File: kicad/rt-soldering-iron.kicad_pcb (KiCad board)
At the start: 2 copper layers, 74.9 x 20.3 mm, 123 parts, among them J1 IRON_TIP, J2 BARREL_JACK, J3 CONN_01X04, Q1 SIA483DJ-T1-GE3, Q2 FDG6301N_F085, Q3 MMBT3904, Q4 MMBT3906WT1G, Q5 FDG6301N_F085, Q6 MMBT3906WT1G, Q7 FDG6301N_F085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

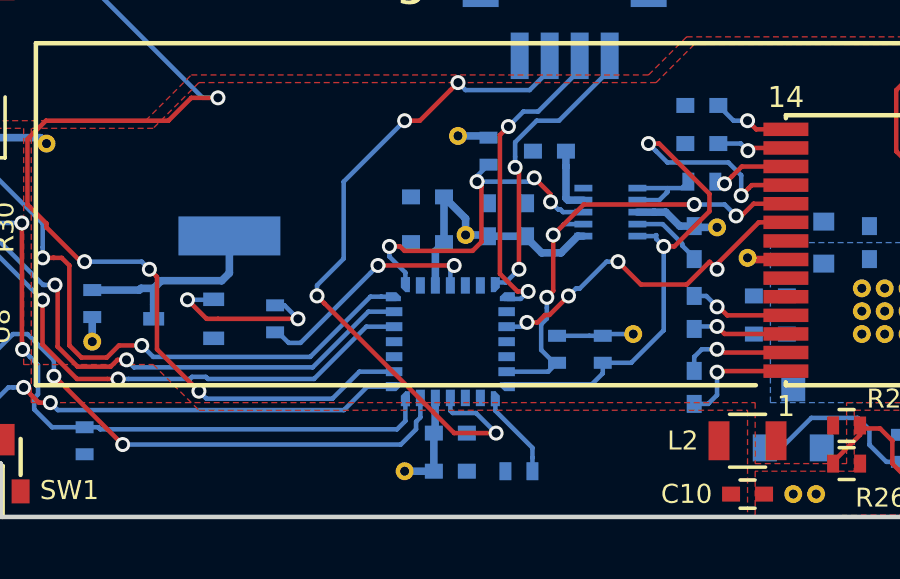
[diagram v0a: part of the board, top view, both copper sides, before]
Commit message: Added tags to unused QFN pins except on accelerometer
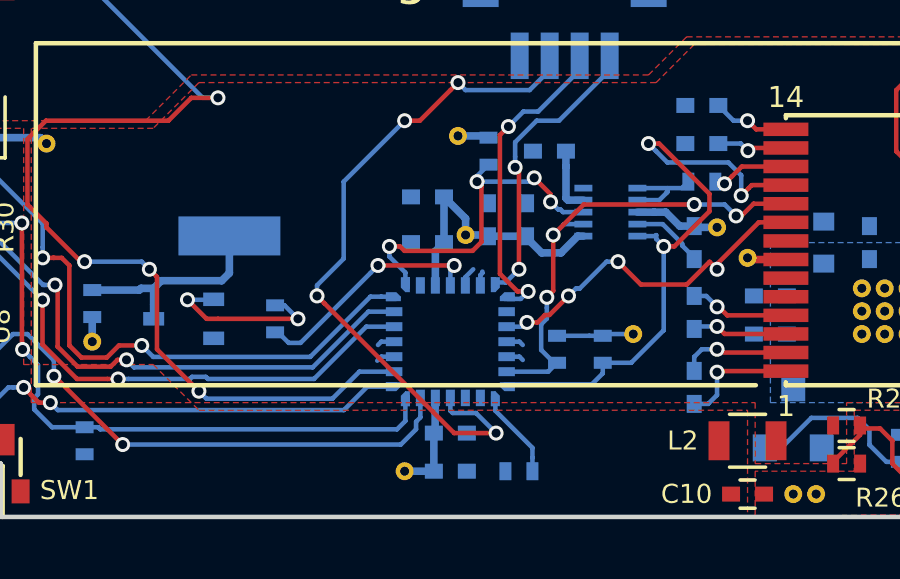
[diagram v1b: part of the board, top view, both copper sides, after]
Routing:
- net Net-(U4-Pad19): track 0.00 -> 0.65 mm
- net Net-(U4-Pad10): track 0.00 -> 0.62 mm
- net Net-(U4-Pad11): track 0.00 -> 0.58 mm
- net Net-(U4-Pad26): track 0.00 -> 0.58 mm
- net Net-(U4-Pad25): track 0.00 -> 0.58 mm
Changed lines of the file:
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@@
     (thickness 1.6)
     (drawings 29)
-    (tracks 739)
+    (tracks 752)
     (zones 0)
     (modules 123)
@@
   (segment (start 163.518 95.504) (end 163.752624 95.504) (width 0.1524) (layer B.Cu) (net 27))
   (via (at 163.82425 95.575626) (size 0.5) (drill 0.3) (layers F.Cu B.Cu) (net 27))
+  (segment (start 155.686 98.963) (end 155.686 98.618066) (width 0.1524) (layer B.Cu) (net 30))
+  (segment (start 155.686 98.618066) (end 155.752809 98.551257) (width 0.1524) (layer B.Cu) (net 30))
+  (segment (start 155.752809 98.551257) (end 155.752809 98.501191) (width 0.1524) (layer B.Cu) (net 30))
   (segment (start 158.623 99.314) (end 158.872999 99.064001) (width 0.1524) (layer B.Cu) (net 32))
   (segment (start 158.872999 99.064001) (end 158.999999 99.064001) (width 0.1524) (layer B.Cu) (net 32))
@@
   (segment (start 156.561 100.338) (end 157.096597 100.338) (width 0.1524) (layer B.Cu) (net 32))
   (segment (start 157.096597 100.338) (end 157.239026 100.195571) (width 0.1524) (layer B.Cu) (net 32))
+  (segment (start 156.561 101.338) (end 156.9884 101.338) (width 0.1524) (layer B.Cu) (net 33))
+  (segment (start 156.9884 101.338) (end 157.099 101.4486) (width 0.1524) (layer B.Cu) (net 33))
   (segment (start 129.667 90.805) (end 129.667 91.636) (width 0.1524) (layer B.Cu) (net 37))
   (segment (start 129.667 91.636) (end 129.725 91.694) (width 0.1524) (layer B.Cu) (net 37))
@@
   (via (at 136.271 102.362) (size 0.5) (drill 0.3) (layers F.Cu B.Cu) (net 59))
   (segment (start 135.578 102.362) (end 136.271 102.362) (width 0.1524) (layer F.Cu) (net 59))
+  (segment (start 155.186 98.687) (end 155.448 98.425) (width 0.1524) (layer B.Cu) (net 60))
+  (segment (start 155.186 98.963) (end 155.186 98.687) (width 0.1524) (layer B.Cu) (net 60))
+  (segment (start 152.811 101.338) (end 152.3836 101.338) (width 0.1524) (layer B.Cu) (net 61))
+  (segment (start 152.3836 101.338) (end 152.2486 101.473) (width 0.1524) (layer B.Cu) (net 61))
+  (segment (start 152.811 100.838) (end 152.3836 100.838) (width 0.1524) (layer B.Cu) (net 62))
+  (segment (start 152.3836 100.838) (end 152.273 100.9486) (width 0.1524) (layer B.Cu) (net 62))
   (segment (start 168.656 104.2804) (end 168.656 103.7724) (width 0.1524) (layer B.Cu) (net 63))
   (segment (start 168.656 103.7724) (end 168.2616 103.378) (width 0.1524) (layer B.Cu) (net 63))
@@
   (segment (start 172.708 102.108) (end 173.482 102.108) (width 0.1524) (layer B.Cu) (net 64))
   (via (at 173.482 102.108) (size 0.5) (drill 0.3) (layers F.Cu B.Cu) (net 64))
+  (segment (start 156.561 100.838) (end 156.9884 100.838) (width 0.1524) (layer B.Cu) (net 65))
+  (segment (start 156.9884 100.838) (end 157.099 100.9486) (width 0.1524) (layer B.Cu) (net 65))
   (zone (net 5) (net_name +12V) (layer F.Cu) (hatch edge 0.508)
     (connect_pads yes (clearance 0.1778))

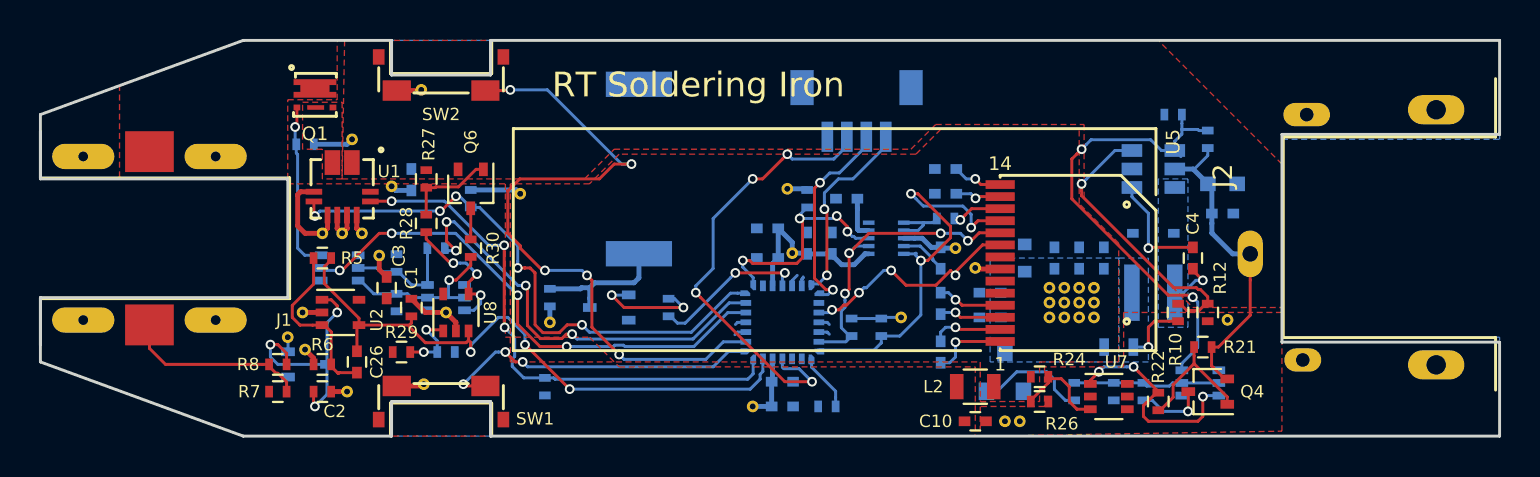
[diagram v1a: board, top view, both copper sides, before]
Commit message: Fixed some capacitor footprints
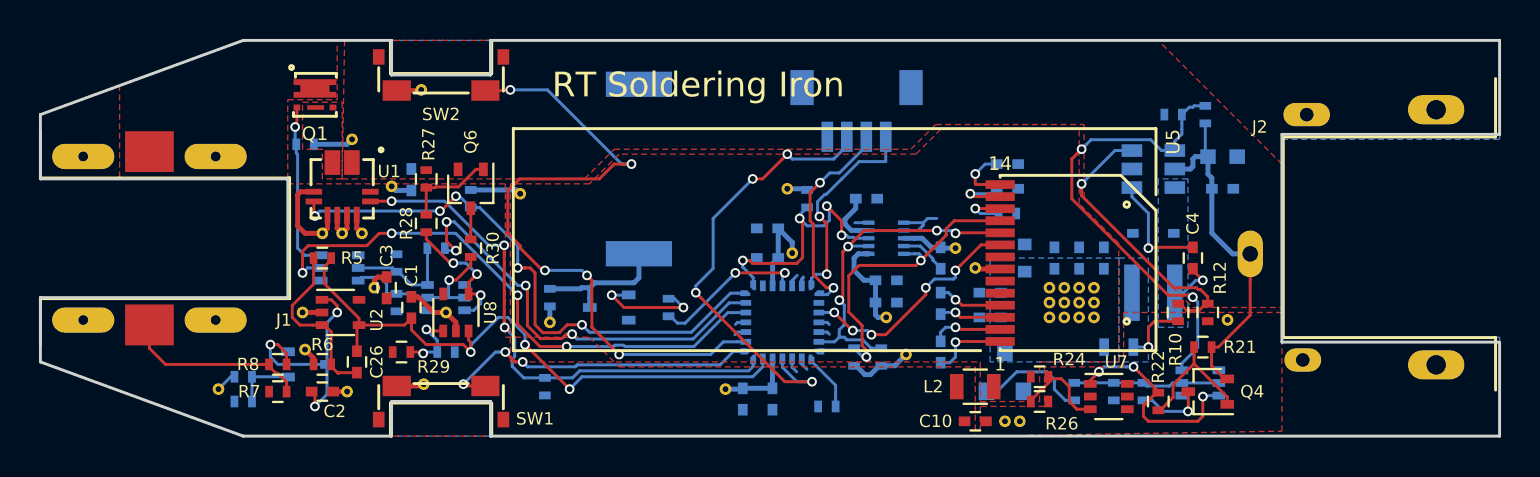
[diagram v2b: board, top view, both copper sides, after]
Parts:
- removed the REF** at (134.0, 97.4)
- removed the REF** at (129.3, 101.6)
- added R34: SPR, Resistors_SMD:R_0402, B.Cu at (127.0, 103.6)
- added R35: 0, Resistors_SMD:R_0402, B.Cu at (127.0, 104.9)
- added REF**: 1PIN-VIA, rt-soldering-iron:1PIN-VIA, F.Cu at (125.7, 104.3)
- added REF**: 1PIN-VIA, rt-soldering-iron:1PIN-VIA, F.Cu at (160.0, 100.6)
- added REF**: 1PIN-VIA, rt-soldering-iron:1PIN-VIA, F.Cu at (133.7, 99.1)
- C1, C2: footprint Resistors_SMD:R_0402 -> Capacitors_SMD:C_0402
- D2: value BAS70-04W -> BAV99WT1G
- moved C21 5.08 mm to (160.0, 99.8), turned to 0 degrees
- moved C22 3.38 mm to (160.0, 98.7), turned to 0 degrees
- moved C19 3.19 mm to (166.2, 92.7), turned to 0 degrees
- moved R18 3.19 mm to (166.2, 95.2), turned to 0 degrees
- moved C20 3.19 mm to (166.2, 94.0), turned to 0 degrees
- moved R16 2.16 mm to (159.8, 102.6), turned to 90 degrees
- moved C14 2.07 mm to (152.7, 104.8), turned to 270 degrees
- moved R15 2.07 mm to (158.4, 102.6), turned to 90 degrees
- moved REF** 1.92 mm to (161.0, 102.5)
- moved REF** 1.66 mm to (151.8, 104.3)
- moved C5 1.40 mm to (177.3, 92.3)
- moved R9 1.28 mm to (176.4, 90.2)
- moved C6 1.27 mm to (177.3, 94.0)
- moved C13 1.02 mm to (154.2, 104.8), turned to 270 degrees
- moved C24 1.02 mm to (159.0, 94.5), turned to 0 degrees
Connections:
- D2 pad 1: GND -> Net-(D2-Pad1)
- D2 pad 2: +3.3VA -> GND
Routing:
- net /Digital Control/I2C_SDA: track 21.2 -> 17.6 mm, vias 3 -> 2
- net Net-(D2-Pad1): track 0.00 -> 3.13 mm
- net /Analog Frontend/HEATER_LATCH_RESET: track 26.7 -> 29.4 mm
- net +12V: track 18.4 -> 20.3 mm
- net +3V3: track 19.0 -> 20.8 mm
- net /Digital Control/I2C_SCL: track 16.2 -> 17.9 mm
- net /Digital Control/ACC_INT: track 11.8 -> 13.3 mm
- net +3.3VA: track 5.29 -> 6.13 mm
- net /Digital Control/STM32_SWDIO: track 9.88 -> 10.7 mm
- net Net-(U4-Pad3): track 0.00 -> 0.76 mm
- net Net-(C24-Pad1): track 2.17 -> 2.89 mm
- net Net-(U6-Pad5): track 0.00 -> 0.71 mm
- net Net-(C20-Pad1): track 2.39 -> 3.05 mm
- net Net-(U4-Pad2): track 0.00 -> 0.65 mm
- net Net-(C19-Pad1): track 2.58 -> 3.11 mm
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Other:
- board text added: "Before sending gerbers, add edge cuts for the oval pins. Do not rebuild the copper pours."
- board text removed: "Before sending gerbers, add edge cuts for the oval pins"
